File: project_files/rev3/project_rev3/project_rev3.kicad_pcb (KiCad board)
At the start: 2 copper layers, 86 x 109 mm, 56 parts, among them J1 Barrel_Jack, J2 Conn_01x04, J3 Conn_01x02, J4 Conn_01x02, J5 Conn_01x02, J6 Conn_01x02, J7 Conn_01x02, J8 USB_C_Receptacle_16P, Q1 BSS816NWH6327XTSA1, Q2 S8550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

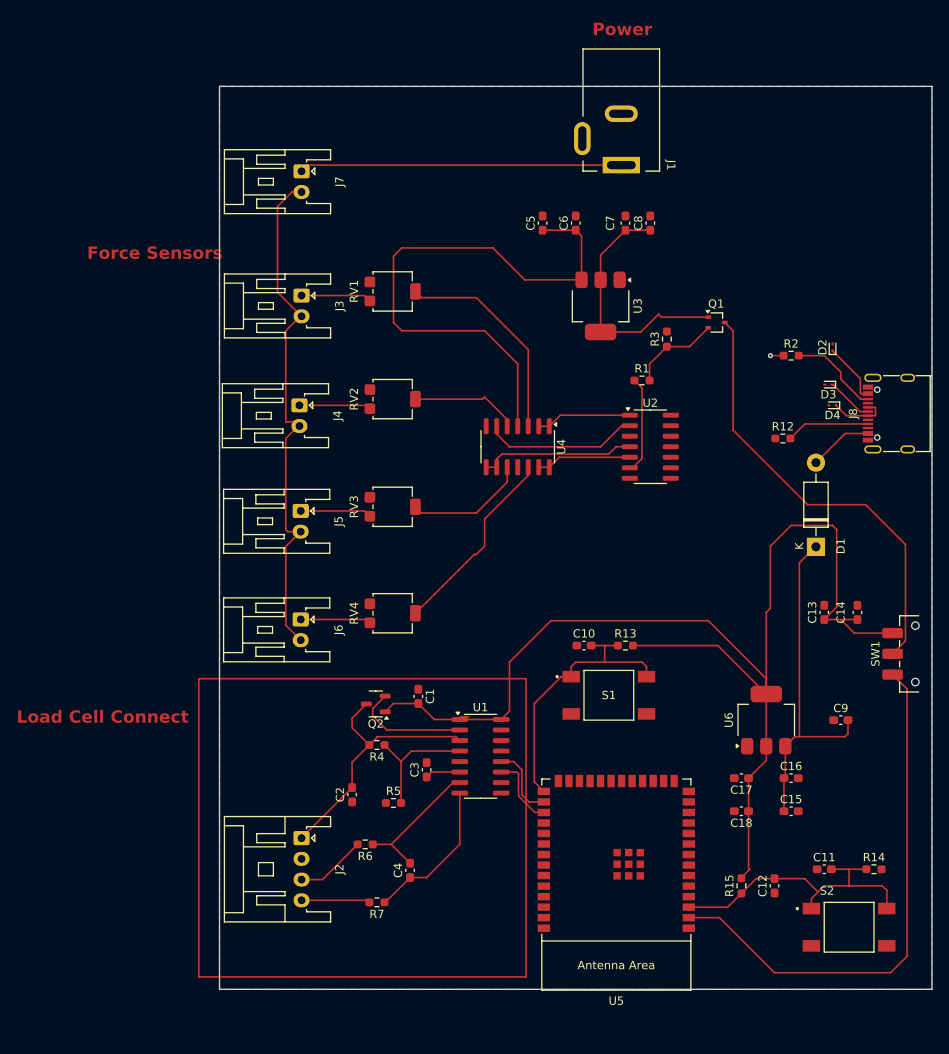
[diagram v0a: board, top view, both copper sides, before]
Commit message: added labels to rev3 sch and pcb
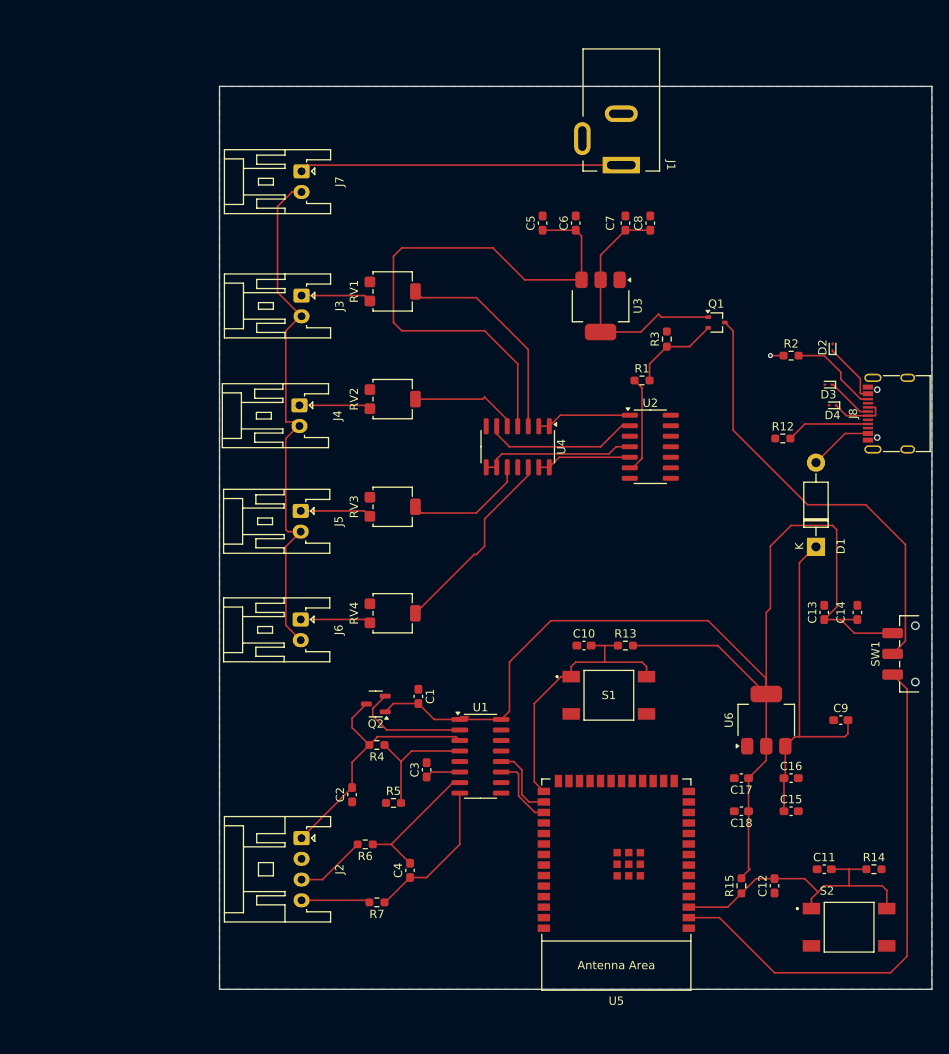
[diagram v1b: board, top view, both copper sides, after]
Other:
- board text added: "Controller/Programmer"
- board text added: "Force Sensor Connections"
- board text added: "Load Cell Connect & ADC"
- board text added: "Power FLOPS"
- board text added: "USB PROG/Power"
- board text removed: "Force Sensors"
- board text removed: "Load Cell Connect"
- board text removed: "Power"
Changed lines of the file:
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@@
-	)
-	(gr_rect
-		(start 37.5 122)
-		(end 77 158)
-		(stroke
-			(width 0.2)
-			(type default)
-		)
-		(fill none)
-		(layer "F.Cu")
 	)
 	(gr_rect
@@
 		(layer "Edge.Cuts")
 	)
-	(gr_text "Force Sensors"
-		(at 24 71.5 0)
-		(layer "F.Cu")
+	(gr_rect
+		(start 35 43.5)
+		(end 56 123.5)
+		(stroke
+			(width 0.1)
+			(type default)
+		)
+		(fill none)
+		(layer "User.1")
+	)
+	(gr_rect
+		(start 77.5 109.5)
+		(end 134 163)
+		(stroke
+			(width 0.1)
+			(type default)
+		)
+		(fill none)
+		(layer "User.1")
+	)
+	(gr_rect
+		(start 78 38.5)
+		(end 102 84)
+		(stroke
+			(width 0.1)
+			(type default)
+		)
+		(fill none)
+		(layer "User.1")
+	)
+	(gr_rect
+		(start 106 76.5)
+		(end 137.5 101)
+		(stroke
+			(width 0.1)
+			(type default)
+		)
+		(fill none)
+		(layer "User.1")
+	)
+	(gr_rect
+		(start 37.5 126)
+		(end 75.5 162.5)
+		(stroke
+			(width 0.1)
+			(type default)
+		)
+		(fill none)
+		(layer "User.1")
+	)
+	(gr_text "Power FLOPS"
+		(at 81.5 43 0)
+		(layer "User.1")
 		(effects
 			(font
-				(size 1.5 1.5)
-				(thickness 0.3)
-				(bold yes)
+				(size 1 1)
+				(thickness 0.15)
 			)
 			(justify left bottom)
 		)
 	)
-	(gr_text "Power"
-		(at 85 44.5 0)
-		(layer "F.Cu")
+	(gr_text "Controller/Programmer"
+		(at 112 161.5 0)
+		(layer "User.1")
 		(effects
 			(font
-				(size 1.5 1.5)
-				(thickness 0.3)
-				(bold yes)
+				(size 1 1)
+				(thickness 0.15)
 			)
 			(justify left bottom)
 		)
 	)
-	(gr_text "Load Cell Connect"
-		(at 15.5 127.5 0)
-		(layer "F.Cu")
+	(gr_text "USB PROG/Power"
+		(at 109 79 0)
+		(layer "User.1")
 		(effects
 			(font
-				(size 1.5 1.5)
-				(thickness 0.3)
-				(bold yes)
+				(size 1 1)
+				(thickness 0.15)
 			)
 			(justify left bottom)
+		)
+	)
+	(gr_text "Load Cell Connect & ADC"
+		(at 46 156.5 0)
+		(layer "User.1")
+		(effects
+			(font
+				(size 1 1)
+				(thickness 0.15)
+			)
+			(justify left bottom)
+		)
+	)
+	(gr_text "Force Sensor Connections"
+		(at 36.5 48.5 0)
+		(layer "User.1")
+		(effects
+			(font
+				(size 1 1)
+				(thickness 0.15)
+			)
+			(justify left bottom)

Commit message: making a commit, didn't mean to do it on main but here we are
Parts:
- removed R12: 5.1k, Resistor_SMD:R_0603_1608Metric_Pad0.98x0.95mm_HandSolder
- removed S1, S2: PTS810SJM250SMTR LFS, TS04-66-95-BK-100-SMT:SW_TS04-66-95-BK-100-SMT
- added R8: 5.1k, Resistor_SMD:R_0603_1608Metric_Pad0.98x0.95mm_HandSolder, F.Cu at (111.5, 85.0)
- added SW2: PTS810 SJM 250 SMTR LFS, PTS810SJM250SMTR LFS:PTS810_CNK, F.Cu at (91.5, 125.5)
- added SW3: PTS810 SJM 250 SMTR LFS, PTS810SJM250SMTR LFS:PTS810_CNK, F.Cu at (116.5, 151.5)
- D1: footprint Diode_THT:D_DO-41_SOD81_P10.16mm_Horizontal -> Diode_SMD:D_SOD-123
- D2, D3, D4: value ESD5B5CU -> ESD9B5.0ST5G
- J8: value USB_C_Receptacle_16P -> USB_C_Receptacle_USB2.0_16P; footprint Connector_USB:USB_C_Receptacle_G-Switch_GT-USB-7010ASV -> Connector_USB:USB_C_Receptacle_GCT_USB4105-xx-A_16P_TopMnt_Horizontal
- moved R2 15.0 mm to (115.5, 96.5), turned to 90 degrees
- moved D3 7.00 mm to (113.5, 93.5), turned to -90 degrees
- moved U5 5.65 mm to (87.9, 149.5)
- moved D4 3.00 mm to (111.0, 89.0)
- moved D1 2.66 mm to (114.5, 107.0), turned to 0 degrees
- moved R3 2.32 mm to (95.2, 83.0)
- moved Q1 2.00 mm to (100.0, 81.0)
- moved C17 1.64 mm to (104.6, 134.0)
- moved C18 1.64 mm to (104.6, 138.0)
- moved C9 1.51 mm to (116.0, 125.9), turned to -90 degrees
- moved R1 1.32 mm to (91.8, 84.9), turned to 90 degrees
- moved U2 1.27 mm to (91.8, 95.2)
- moved J1 1.12 mm to (88.1, 59.0)
- moved J8 1.03 mm to (121.8, 89.0)
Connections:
- net Net-(D1-A) renamed /controller/VBUS
- net Net-(D3-A1) renamed /controller/USB_D-
- net Net-(D4-A1) renamed /controller/USB_D+
- J8 pad A5: Net-(J8-CC1) -> /controller/CC1
- J8 pad B5: Net-(J8-CC2) -> /controller/CC2
- R2 pad 2: Net-(J8-CC2) -> /controller/CC1
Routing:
- net /controller/USB_D-: track 5.70 -> 72.3 mm
- net /controller/USB_D+: track 7.15 -> 70.5 mm
- net GND: track 1.59 -> 54.4 mm, vias 1 -> 53
- net ESP_3.3V: track 153.2 -> 122.4 mm, vias 0 -> 2
- net +5V_WALL: track 130.9 -> 158.4 mm
- net /controller/VBUS: track 15.2 -> 31.0 mm, vias 0 -> 2
- net GPIO0_BOOT: track 34.1 -> 45.2 mm
- net Net-(J8-CC2): track 11.0 -> 0.00 mm
- net Net-(J8-CC1): track 10.1 -> 0.00 mm
- net Net-(Q1-G): track 10.9 -> 2.22 mm
- net /controller/CC2: track 0.00 -> 8.01 mm
- net /controller/CC1: track 0.00 -> 7.38 mm
- net GPIO_35: track 8.93 -> 14.5 mm
- net GPIO_36: track 8.73 -> 14.3 mm
- net CHIP_PU_EN: track 37.3 -> 40.5 mm
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
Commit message: added new project for rev4 and reverted changes for rev3
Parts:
- removed R8: 5.1k, Resistor_SMD:R_0603_1608Metric_Pad0.98x0.95mm_HandSolder
- removed SW2, SW3: PTS810 SJM 250 SMTR LFS, PTS810SJM250SMTR LFS:PTS810_CNK
- added R12: 5.1k, Resistor_SMD:R_0603_1608Metric_Pad0.98x0.95mm_HandSolder, F.Cu at (108.0, 93.0)
- added S1: PTS810SJM250SMTR LFS, TS04-66-95-BK-100-SMT:SW_TS04-66-95-BK-100-SMT, F.Cu at (87.0, 124.0)
- added S2: PTS810SJM250SMTR LFS, TS04-66-95-BK-100-SMT:SW_TS04-66-95-BK-100-SMT, F.Cu at (116.0, 152.0)
- D1: footprint Diode_SMD:D_SOD-123 -> Diode_THT:D_DO-41_SOD81_P10.16mm_Horizontal
- D2, D3, D4: value ESD9B5.0ST5G -> ESD5B5CU
- J8: value USB_C_Receptacle_USB2.0_16P -> USB_C_Receptacle_16P; footprint Connector_USB:USB_C_Receptacle_GCT_USB4105-xx-A_16P_TopMnt_Horizontal -> Connector_USB:USB_C_Receptacle_G-Switch_GT-USB-7010ASV
- moved R2 15.0 mm to (109.0, 83.0), turned to 0 degrees
- moved D3 7.00 mm to (113.5, 86.5), turned to 180 degrees
- moved U5 5.65 mm to (87.9, 143.9)
- moved D4 3.00 mm to (114.0, 89.0)
- moved D1 2.66 mm to (112.0, 106.1), turned to 90 degrees
- moved R3 2.32 mm to (94.0, 81.0)
- moved Q1 2.00 mm to (100.0, 79.0)
- moved C17 1.64 mm to (103.0, 134.0)
- moved C18 1.64 mm to (103.0, 138.0)
- moved C9 1.51 mm to (115.0, 127.0), turned to 0 degrees
- moved R1 1.32 mm to (91.0, 86.0), turned to 0 degrees
- moved U2 1.27 mm to (92.0, 94.0)
- moved J1 1.12 mm to (88.5, 60.0)
- moved J8 1.03 mm to (122.0, 90.0)
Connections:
- net /controller/USB_D+ renamed Net-(D4-A1)
- net /controller/USB_D- renamed Net-(D3-A1)
- net /controller/VBUS renamed Net-(D1-A)
- J8 pad A5: /controller/CC1 -> Net-(J8-CC1)
- J8 pad B5: /controller/CC2 -> Net-(J8-CC2)
- R2 pad 2: /controller/CC1 -> Net-(J8-CC2)
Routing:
- net Net-(D3-A1): track 72.3 -> 5.70 mm
- net Net-(D4-A1): track 70.5 -> 7.15 mm
- net GND: track 54.4 -> 1.59 mm, vias 53 -> 1
- net ESP_3.3V: track 122.4 -> 153.2 mm, vias 2 -> 0
- net +5V_WALL: track 158.4 -> 130.9 mm
- net Net-(D1-A): track 31.0 -> 15.2 mm, vias 2 -> 0
- net GPIO0_BOOT: track 45.2 -> 34.1 mm
- net Net-(J8-CC2): track 0.00 -> 11.0 mm
- net Net-(J8-CC1): track 0.00 -> 10.1 mm
- net Net-(Q1-G): track 2.22 -> 10.9 mm
- net /controller/CC2: track 8.01 -> 0.00 mm
- net /controller/CC1: track 7.38 -> 0.00 mm
- net GPIO_35: track 14.5 -> 8.93 mm
- net GPIO_36: track 14.3 -> 8.73 mm
- net CHIP_PU_EN: track 40.5 -> 37.3 mm
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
